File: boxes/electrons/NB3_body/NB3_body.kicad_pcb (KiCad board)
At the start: 2 copper layers, 200 x 199.5 mm, 36 parts, among them J1 Conn_02x05_Counter_Clockwise, J10 Conn_02x03_Top_Bottom, J11 Conn_02x03_Top_Bottom, J12 Conn_02x03_Top_Bottom, J13 JST ZH 6-way Socket, J14 JST ZH 6-way Socket, J2 Conn_02x05_Counter_Clockwise, J3 Conn_02x05_Counter_Clockwise, J4 Conn_02x05_Counter_Clockwise, J5 Conn_02x05_Counter_Clockwise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

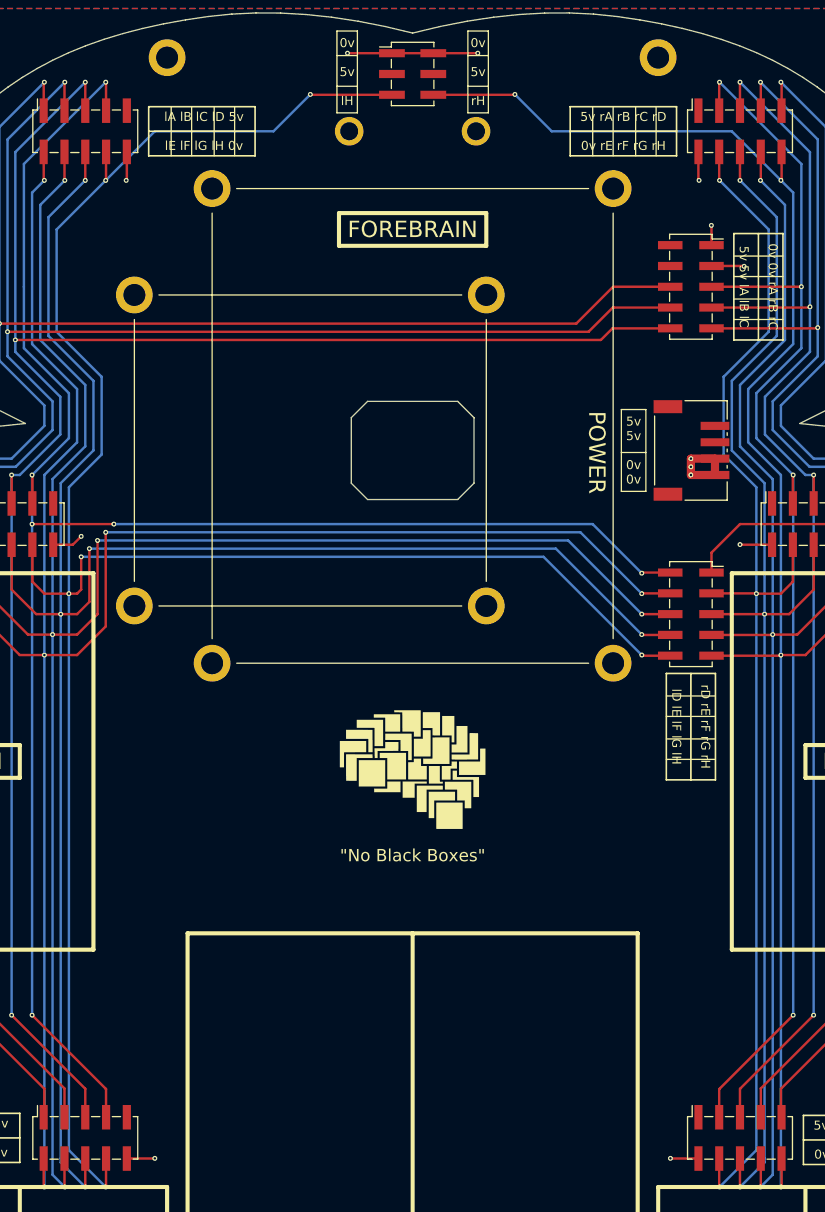
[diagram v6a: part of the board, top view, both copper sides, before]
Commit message: Submitted NB3_body PCB
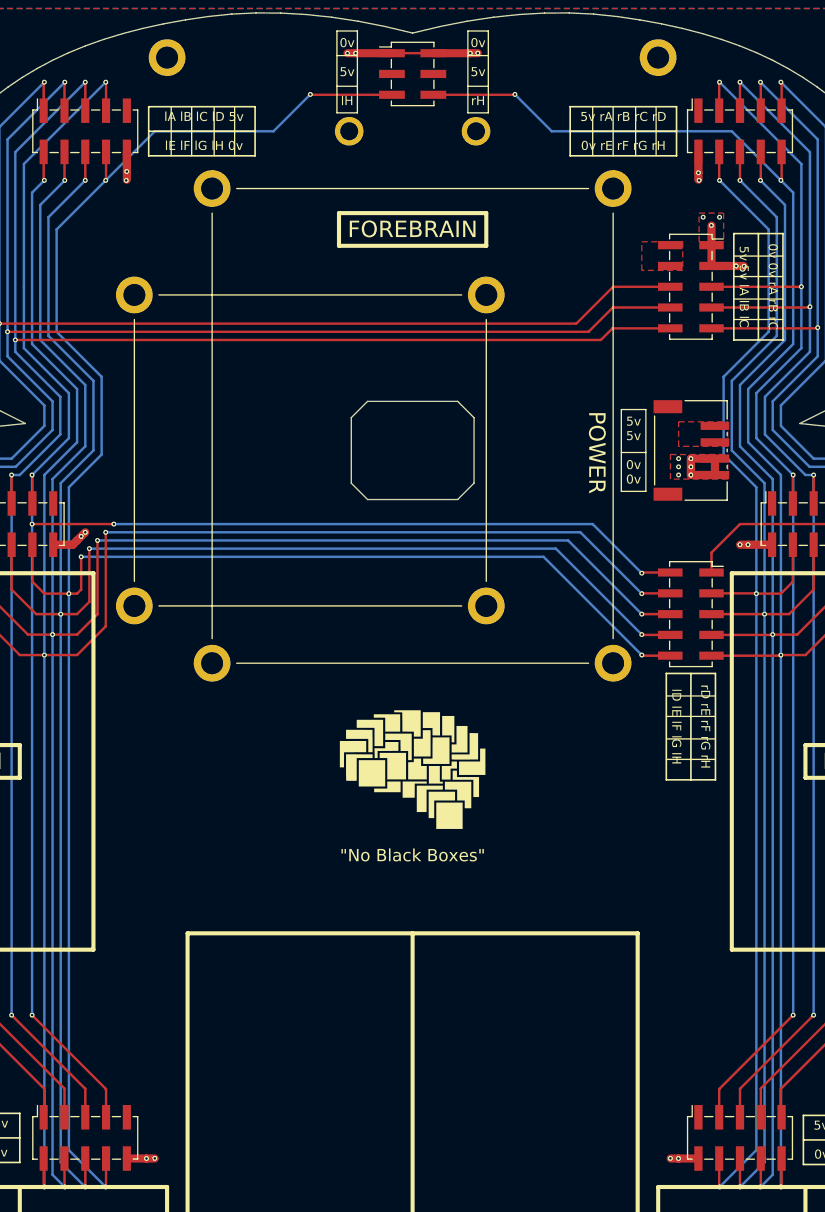
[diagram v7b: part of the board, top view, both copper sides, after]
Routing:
- net GND: track 54.0 -> 57.2 mm, vias 13 -> 27
- added copper zone on F.Cu, net GND
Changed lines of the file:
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@@
       (sketchpadsonfab false)
       (subtractmaskfromsilk false)
-      (outputformat 1)
+      (outputformat 3)
       (mirror false)
       (drillshape 0)
@@
   (segment (start 79.5 80) (end 83.5 76) (width 0.3) (layer "B.Cu") (net 9))
   (segment (start 158.5 78) (end 158.5 79) (width 1) (layer "F.Cu") (net 10))
-  (segment (start 89.58 40.52) (end 89.58 43.92) (width 0.3) (layer "F.Cu") (net 10))
+  (segment (start 89.58 40.52) (end 89.58 42.92) (width 1) (layer "F.Cu") (net 10))
+  (segment (start 83.5 88) (end 82.98 88.52) (width 1) (layer "F.Cu") (net 10))
   (segment (start 89.58 43.92) (end 89.5 44) (width 0.3) (layer "F.Cu") (net 10))
+  (segment (start 159.42 43.08) (end 159.42 43.92) (width 1) (layer "F.Cu") (net 10))
+  (segment (start 164.04 54.46) (end 164.96 54.46) (width 1) (layer "F.Cu") (net 10))
   (segment (start 164.96 54.46) (end 165 54.5) (width 0.3) (layer "F.Cu") (net 10))
   (segment (start 161.444701 77.999999) (end 158.5 78) (width 1) (layer "F.Cu") (net 10))
-  (segment (start 89.58 163.52) (end 92.98 163.52) (width 0.3) (layer "F.Cu") (net 10))
+  (segment (start 84.5 87) (end 83.5 88) (width 1) (layer "F.Cu") (net 10))
+  (segment (start 89.58 163.52) (end 91.98 163.52) (width 1) (layer "F.Cu") (net 10))
+  (segment (start 89.58 42.92) (end 89.58 43.92) (width 1) (layer "F.Cu") (net 10))
   (segment (start 164.52 88.52) (end 164.5 88.5) (width 0.3) (layer "F.Cu") (net 10))
   (segment (start 156.02 163.52) (end 156 163.5) (width 0.3) (layer "F.Cu") (net 10))
   (segment (start 161.444701 77.999999) (end 161.444701 79.999998) (width 1) (layer "F.Cu") (net 10))
   (segment (start 159.42 43.92) (end 159.5 44) (width 0.3) (layer "F.Cu") (net 10))
+  (segment (start 131.54 28.46) (end 132.46 28.46) (width 1) (layer "F.Cu") (net 10))
   (segment (start 161.02 49.52) (end 161 49.5) (width 0.3) (layer "F.Cu") (net 10))
-  (segment (start 82.98 88.52) (end 80.58 88.52) (width 0.3) (layer "F.Cu") (net 10))
-  (segment (start 159.42 40.52) (end 159.42 43.92) (width 0.3) (layer "F.Cu") (net 10))
-  (segment (start 159.42 163.52) (end 156.02 163.52) (width 0.3) (layer "F.Cu") (net 10))
-  (segment (start 84 87.5) (end 82.98 88.52) (width 0.3) (layer "F.Cu") (net 10))
-  (segment (start 161.02 54.46) (end 164.96 54.46) (width 0.3) (layer "F.Cu") (net 10))
+  (segment (start 156.98 163.52) (end 156.02 163.52) (width 1) (layer "F.Cu") (net 10))
+  (segment (start 82.98 88.52) (end 80.58 88.52) (width 1) (layer "F.Cu") (net 10))
+  (segment (start 159.42 40.52) (end 159.42 43.08) (width 1) (layer "F.Cu") (net 10))
+  (segment (start 159.42 163.52) (end 156.98 163.52) (width 1) (layer "F.Cu") (net 10))
+  (segment (start 161.02 54.46) (end 164.04 54.46) (width 1) (layer "F.Cu") (net 10))
   (segment (start 158.5 80) (end 158.500002 79.999998) (width 0.3) (layer "F.Cu") (net 10))
   (segment (start 116.54 28.46) (end 116.5 28.5) (width 0.3) (layer "F.Cu") (net 10))
-  (segment (start 121.975 28.46) (end 116.54 28.46) (width 0.3) (layer "F.Cu") (net 10))
+  (segment (start 121.975 28.46) (end 117.54 28.46) (width 1) (layer "F.Cu") (net 10))
+  (segment (start 161.02 51.92) (end 161.02 54.46) (width 1) (layer "F.Cu") (net 10))
   (segment (start 92.98 163.52) (end 93 163.5) (width 0.3) (layer "F.Cu") (net 10))
   (segment (start 158.5 79) (end 158.5 80) (width 1) (layer "F.Cu") (net 10))
-  (segment (start 127.025 28.46) (end 132.46 28.46) (width 0.3) (layer "F.Cu") (net 10))
-  (segment (start 168.42 88.52) (end 164.52 88.52) (width 0.3) (layer "F.Cu") (net 10))
-  (segment (start 161.02 51.92) (end 161.02 49.52) (width 0.3) (layer "F.Cu") (net 10))
+  (segment (start 127.025 28.46) (end 131.54 28.46) (width 1) (layer "F.Cu") (net 10))
+  (segment (start 165.48 88.52) (end 164.52 88.52) (width 1) (layer "F.Cu") (net 10))
+  (segment (start 168.42 88.52) (end 165.48 88.52) (width 1) (layer "F.Cu") (net 10))
+  (segment (start 161.02 51.92) (end 161.02 49.52) (width 1) (layer "F.Cu") (net 10))
+  (segment (start 117.54 28.46) (end 116.54 28.46) (width 1) (layer "F.Cu") (net 10))
   (segment (start 121.975 28.46) (end 127.025 28.46) (width 0.3) (layer "F.Cu") (net 10))
   (segment (start 158.500002 79.999998) (end 161.444701 79.999998) (width 1) (layer "F.Cu") (net 10))
   (segment (start 132.46 28.46) (end 132.5 28.5) (width 0.3) (layer "F.Cu") (net 10))
+  (segment (start 91.98 163.52) (end 92.98 163.52) (width 1) (layer "F.Cu") (net 10))
   (via (at 89.5 44) (size 0.6) (drill 0.3) (layers "F.Cu" "B.Cu") (net 10))
+  (via (at 84.5 87) (size 0.6) (drill 0.3) (layers "F.Cu" "B.Cu") (net 10))
+  (via (at 159.42 43.08) (size 0.6) (drill 0.3) (layers "F.Cu" "B.Cu") (net 10))
+  (via (at 160 48.5) (size 0.6) (drill 0.3) (layers "F.Cu" "B.Cu") (free) (net 10))
+  (via (at 89.58 42.92) (size 0.6) (drill 0.3) (layers "F.Cu" "B.Cu") (net 10))
   (via (at 116.54 28.46) (size 0.6) (drill 0.3) (layers "F.Cu" "B.Cu") (net 10))
+  (via (at 164.04 54.46) (size 0.6) (drill 0.3) (layers "F.Cu" "B.Cu") (net 10))
   (via (at 159.5 44) (size 0.6) (drill 0.3) (layers "F.Cu" "B.Cu") (net 10))
+  (via (at 156.98 163.52) (size 0.6) (drill 0.3) (layers "F.Cu" "B.Cu") (net 10))
+  (via (at 162 48.5) (size 0.6) (drill 0.3) (layers "F.Cu" "B.Cu") (free) (net 10))
   (via (at 84 87.5) (size 0.6) (drill 0.3) (layers "F.Cu" "B.Cu") (net 10))
   (via (at 93 163.5) (size 0.6) (drill 0.3) (layers "F.Cu" "B.Cu") (net 10))
   (via (at 165 54.5) (size 0.6) (drill 0.3) (layers "F.Cu" "B.Cu") (net 10))
+  (via (at 131.54 28.46) (size 0.6) (drill 0.3) (layers "F.Cu" "B.Cu") (net 10))
   (via (at 158.5 80) (size 0.6) (drill 0.3) (layers "F.Cu" "B.Cu") (net 10))
+  (via (at 165.48 88.52) (size 0.6) (drill 0.3) (layers "F.Cu" "B.Cu") (net 10))
+  (via (at 157 80) (size 0.6) (drill 0.3) (layers "F.Cu" "B.Cu") (free) (net 10))
   (via (at 158.5 78) (size 0.6) (drill 0.3) (layers "F.Cu" "B.Cu") (net 10))
+  (via (at 157 78) (size 0.6) (drill 0.3) (layers "F.Cu" "B.Cu") (free) (net 10))
   (via (at 158.5 79) (size 0.6) (drill 0.3) (layers "F.Cu" "B.Cu") (net 10))
   (via (at 161 49.5) (size 0.6) (drill 0.3) (layers "F.Cu" "B.Cu") (net 10))
   (via (at 164.5 88.5) (size 0.6) (drill 0.3) (layers "F.Cu" "B.Cu") (net 10))
+  (via (at 117.54 28.46) (size 0.6) (drill 0.3) (layers "F.Cu" "B.Cu") (net 10))
   (via (at 156 163.5) (size 0.6) (drill 0.3) (layers "F.Cu" "B.Cu") (net 10))
+  (via (at 91.98 163.52) (size 0.6) (drill 0.3) (layers "F.Cu" "B.Cu") (net 10))
   (via (at 132.46 28.46) (size 0.6) (drill 0.3) (layers "F.Cu" "B.Cu") (net 10))
+  (via (at 157 79) (size 0.6) (drill 0.3) (layers "F.Cu" "B.Cu") (free) (net 10))
   (segment (start 162 155) (end 161.96 155.04) (width 0.3) (layer "F.Cu") (net 11))
   (segment (start 161.96 35.48) (end 161.96 32.04) (width 0.3) (layer "F.Cu") (net 11))
@@
   (segment (start 211 174) (end 222.5 185.5) (width 0.3) (layer "F.Cu") (net 30))
   (zone (net 1) (net_name "+5V") (layer "F.Cu") (hatch edge 0.508)
+    (priority 2)
+    (connect_pads yes (clearance 0.5))
+    (min_thickness 0.254) (filled_areas_thickness no)
+    (fill yes (thermal_gap 0.508) (thermal_bridge_width 0.508))
+    (polygon
+      (pts
+        (xy 163 76.5)
+        (xy 157 76.5)
+        (xy 157 73.5)
+        (xy 163 73.5)
+      )
+    )
+  )
+  (zone (net 10) (net_name "GND") (layer "F.Cu") (hatch edge 0.508)
+    (priority 2)
+    (connect_pads yes (clearance 0.5))
+    (min_thickness 0.254) (filled_areas_thickness no)
+    (fill yes (thermal_gap 0.508) (thermal_bridge_width 0.508))
+    (polygon
+      (pts
+        (xy 162.5 51.5)
+        (xy 159.5 51.5)
+        (xy 159.5 48)
+        (xy 162.5 48)
+      )
+    )
+  )
+  (zone (net 1) (net_name "+5V") (layer "F.Cu") (hatch edge 0.508)
+    (priority 2)
+    (connect_pads yes (clearance 0.5))
+    (min_thickness 0.254) (filled_areas_thickness no)
+    (fill yes (thermal_gap 0.508) (thermal_bridge_width 0.508))
+    (polygon
+      (pts
+        (xy 157.5 55)
+        (xy 152.5 55)
+        (xy 152.5 51.5)
+        (xy 157.5 51.5)
+      )
+    )
+  )
+  (zone (net 1) (net_name "+5V") (layer "F.Cu") (hatch edge 0.508)
     (priority 1)
     (connect_pads (clearance 0.5))
@@
       )
     )
+  )
+  (zone (net 10) (net_name "GND") (layer "F.Cu") (hatch edge 0.508)
+    (priority 2)
+    (connect_pads yes (clearance 0.5))
+    (min_thickness 0.254) (filled_areas_thickness no)
+    (fill yes (thermal_gap 0.508) (thermal_bridge_width 0.508))
+    (polygon
+      (pts
+        (xy 163 80.5)
+        (xy 156 80.5)
+        (xy 156 77.5)
+        (xy 163 77.5)
+      )
+    )
